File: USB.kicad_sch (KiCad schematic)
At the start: 8 parts, among them J7 USB-C, U8 USBLC6-2SC6

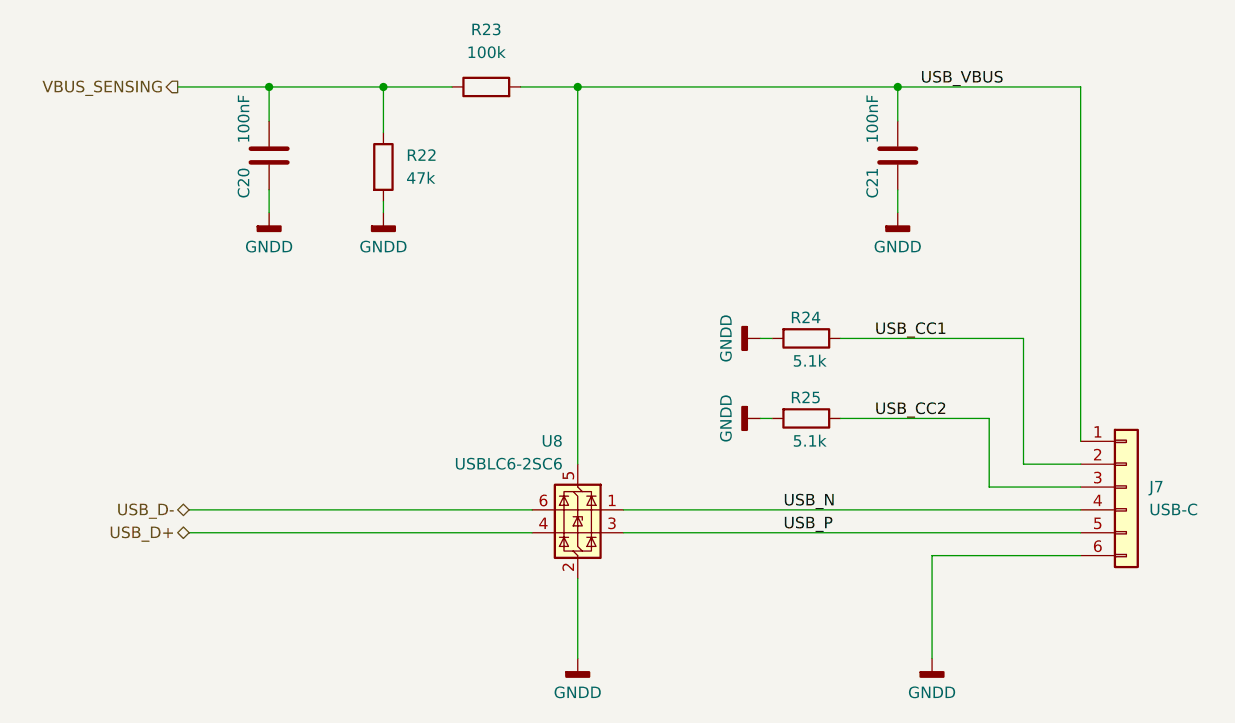
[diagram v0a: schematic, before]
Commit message: USB connector inversion fix
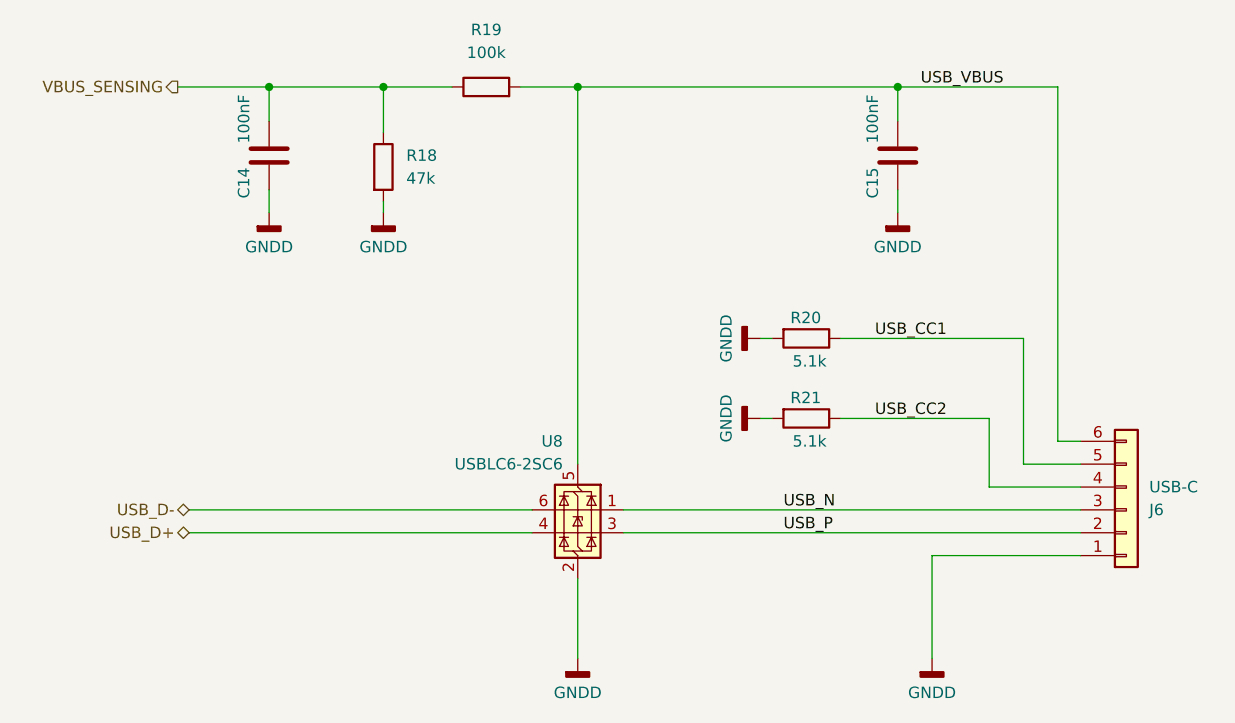
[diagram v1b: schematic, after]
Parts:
- renumbered C20 to C14, C21 to C15, J7 to J6, R22 to R18, R23 to R19, R24 to R20, R25 to R21
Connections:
- net GNDD: now also J6.1 (Pin_1); no longer J6.6 (Pin_6)
- net USB_CC1: now also J6.5 (Pin_5); no longer J6.2 (Pin_2)
- net USB_CC2: now also J6.4 (Pin_4); no longer J6.3 (Pin_3)
- net USB_N: now also J6.3 (Pin_3); no longer J6.4 (Pin_4)
- net USB_P: now also J6.2 (Pin_2); no longer J6.5 (Pin_5)
- net USB_VBUS: now also J6.6 (Pin_6); no longer J6.1 (Pin_1)
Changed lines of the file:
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@@
+	(wire
+		(pts
+			(xy 167.64 100.33) (xy 184.15 100.33)
+		)
+		(stroke
+			(width 0)
+			(type default)
+		)
+	)
+	(wire
+		(pts
+			(xy 83.82 48.26) (xy 106.68 48.26)
+		)
+		(stroke
+			(width 0)
+			(type default)
+		)
+	)
+	(wire
+		(pts
+			(xy 128.27 48.26) (xy 163.83 48.26)
+		)
+		(stroke
+			(width 0)
+			(type default)
+		)
+	)
+	(wire
+		(pts
+			(xy 128.27 102.87) (xy 128.27 111.76)
+		)
+		(stroke
+			(width 0)
+			(type default)
+		)
+	)
+	(wire
+		(pts
+			(xy 181.61 48.26) (xy 181.61 87.63)
+		)
+		(stroke
+			(width 0)
+			(type default)
+		)
+	)
+	(wire
+		(pts
+			(xy 157.48 85.09) (xy 173.99 85.09)
+		)
+		(stroke
+			(width 0)
+			(type default)
+		)
+	)
+	(wire
+		(pts
+			(xy 173.99 92.71) (xy 184.15 92.71)
+		)
+		(stroke
+			(width 0)
+			(type default)
+		)
+	)
+	(wire
+		(pts
+			(xy 121.92 48.26) (xy 128.27 48.26)
+		)
+		(stroke
+			(width 0)
+			(type default)
+		)
+	)
+	(wire
+		(pts
+			(xy 163.83 59.69) (xy 163.83 62.23)
+		)
+		(stroke
+			(width 0)
+			(type default)
+		)
+	)
 	(wire
 		(pts
@@
 	(wire
 		(pts
-			(xy 83.82 48.26) (xy 106.68 48.26)
-		)
-		(stroke
-			(width 0)
-			(type default)
-		)
-	)
-	(wire
-		(pts
-			(xy 128.27 48.26) (xy 163.83 48.26)
-		)
-		(stroke
-			(width 0)
-			(type default)
-		)
-	)
-	(wire
-		(pts
-			(xy 128.27 102.87) (xy 128.27 111.76)
-		)
-		(stroke
-			(width 0)
-			(type default)
-		)
-	)
-	(wire
-		(pts
-			(xy 184.15 48.26) (xy 184.15 87.63)
-		)
-		(stroke
-			(width 0)
-			(type default)
-		)
-	)
-	(wire
-		(pts
-			(xy 157.48 85.09) (xy 173.99 85.09)
-		)
-		(stroke
-			(width 0)
-			(type default)
-		)
-	)
-	(wire
-		(pts
-			(xy 121.92 48.26) (xy 128.27 48.26)
-		)
-		(stroke
-			(width 0)
-			(type default)
-		)
-	)
-	(wire
-		(pts
-			(xy 173.99 92.71) (xy 184.15 92.71)
-		)
-		(stroke
-			(width 0)
-			(type default)
-		)
-	)
-	(wire
-		(pts
-			(xy 163.83 59.69) (xy 163.83 62.23)
-		)
-		(stroke
-			(width 0)
-			(type default)
-		)
-	)
-	(wire
-		(pts
 			(xy 157.48 76.2) (xy 177.8 76.2)
 		)
@@
 	(wire
 		(pts
-			(xy 184.15 48.26) (xy 163.83 48.26)
+			(xy 181.61 48.26) (xy 163.83 48.26)
+		)
+		(stroke
+			(width 0)
+			(type default)
+		)
+	)
+	(wire
+		(pts
+			(xy 181.61 87.63) (xy 184.15 87.63)
 		)
 		(stroke
@@
 	(wire
 		(pts
+			(xy 133.35 97.79) (xy 184.15 97.79)
+		)
+		(stroke
+			(width 0)
+			(type default)
+		)
+	)
+	(wire
+		(pts
 			(xy 149.86 76.2) (xy 148.59 76.2)
 		)
@@
 	(wire
 		(pts
-			(xy 133.35 97.79) (xy 184.15 97.79)
-		)
-		(stroke
-			(width 0)
-			(type default)
-		)
-	)
-	(wire
-		(pts
 			(xy 114.3 48.26) (xy 106.68 48.26)
 		)
@@
 		(pts
 			(xy 93.98 48.26) (xy 93.98 52.07)
-		)
-		(stroke
-			(width 0)
-			(type default)
-		)
-	)
-	(wire
-		(pts
-			(xy 167.64 100.33) (xy 184.15 100.33)
 		)
 		(stroke
@@
 		(dnp no)
 		(fields_autoplaced yes)
-		(property "Reference" "#PWR036"
+		(property "Reference" "#PWR032"
 			(at 142.24 85.09 0)
 			(hide yes)
@@
 			(project "GSMreceiver"
 				(path "/bbc92722-7b85-49e8-a662-589426df605a/e36e7992-f69d-4591-9880-6ae3c36efe0e"
-					(reference "#PWR036")
+					(reference "#PWR032")
 					(unit 1)
 				)
@@
 		(dnp no)
 		(fields_autoplaced yes)
-		(property "Reference" "#PWR034"
+		(property "Reference" "#PWR030"
 			(at 128.27 118.11 0)
 			(hide yes)
@@
 			(project "GSMreceiver"
 				(path "/bbc92722-7b85-49e8-a662-589426df605a/e36e7992-f69d-4591-9880-6ae3c36efe0e"
-					(reference "#PWR034")
+					(reference "#PWR030")
 					(unit 1)
 				)
@@
 		(dnp no)
 		(fields_autoplaced yes)
-		(property "Reference" "#PWR032"
+		(property "Reference" "#PWR028"
 			(at 93.98 68.58 0)
 			(hide yes)
@@
 			(project "GSMreceiver"
 				(path "/bbc92722-7b85-49e8-a662-589426df605a/e36e7992-f69d-4591-9880-6ae3c36efe0e"
-					(reference "#PWR032")
+					(reference "#PWR028")
 					(unit 1)
 				)
@@
 		(dnp no)
 		(fields_autoplaced yes)
-		(property "Reference" "R23"
+		(property "Reference" "R19"
 			(at 118.11 41.91 90)
 			(show_name no)
@@
 			(project "GSMreceiver"
 				(path "/bbc92722-7b85-49e8-a662-589426df605a/e36e7992-f69d-4591-9880-6ae3c36efe0e"
-					(reference "R23")
+					(reference "R19")
 					(unit 1)
 				)
@@
 		(in_pos_files yes)
 		(dnp no)
-		(property "Reference" "C20"
+		(property "Reference" "C14"
 			(at 91.186 58.928 90)
 			(show_name no)
@@
 			(project "GSMreceiver"
 				(path "/bbc92722-7b85-49e8-a662-589426df605a/e36e7992-f69d-4591-9880-6ae3c36efe0e"
-					(reference "C20")
+					(reference "C14")
 					(unit 1)
 				)
@@
 		(dnp no)
 		(fields_autoplaced yes)
-		(property "Reference" "R22"
+		(property "Reference" "R18"
 			(at 109.22 55.8799 0)
 			(show_name no)
@@
 			(project "GSMreceiver"
 				(path "/bbc92722-7b85-49e8-a662-589426df605a/e36e7992-f69d-4591-9880-6ae3c36efe0e"
-					(reference "R22")
+					(reference "R18")
 					(unit 1)
 				)
@@
 		(dnp no)
 		(fields_autoplaced yes)
-		(property "Reference" "#PWR033"
+		(property "Reference" "#PWR029"
 			(at 106.68 68.58 0)
 			(hide yes)
@@
 			(project "GSMreceiver"
 				(path "/bbc92722-7b85-49e8-a662-589426df605a/e36e7992-f69d-4591-9880-6ae3c36efe0e"
-					(reference "#PWR033")
+					(reference "#PWR029")
 					(unit 1)
 				)
@@
 		(in_pos_files yes)
 		(dnp no)
-		(property "Reference" "C21"
+		(property "Reference" "C15"
 			(at 161.036 58.928 90)
 			(show_name no)
@@
 			(project "GSMreceiver"
 				(path "/bbc92722-7b85-49e8-a662-589426df605a/e36e7992-f69d-4591-9880-6ae3c36efe0e"
-					(reference "C21")
+					(reference "C15")
 					(unit 1)
 				)
@@
 		(dnp no)
 		(fields_autoplaced yes)
-		(property "Reference" "#PWR037"
+		(property "Reference" "#PWR033"
 			(at 163.83 68.58 0)
 			(hide yes)
@@
 			(project "GSMreceiver"
 				(path "/bbc92722-7b85-49e8-a662-589426df605a/e36e7992-f69d-4591-9880-6ae3c36efe0e"
-					(reference "#PWR037")
+					(reference "#PWR033")
 					(unit 1)
 				)
@@
 		(dnp no)
 		(fields_autoplaced yes)
-		(property "Reference" "#PWR038"
+		(property "Reference" "#PWR034"
 			(at 167.64 118.11 0)
 			(hide yes)
@@
 			(project "GSMreceiver"
 				(path "/bbc92722-7b85-49e8-a662-589426df605a/e36e7992-f69d-4591-9880-6ae3c36efe0e"
-					(reference "#PWR038")
+					(reference "#PWR034")
 					(unit 1)
 				)
@@
 		(in_pos_files yes)
 		(dnp no)
-		(property "Reference" "R25"
+		(property "Reference" "R21"
 			(at 151.892 82.804 90)
 			(show_name no)
@@
 			(project "GSMreceiver"
 				(path "/bbc92722-7b85-49e8-a662-589426df605a/e36e7992-f69d-4591-9880-6ae3c36efe0e"
-					(reference "R25")
+					(reference "R21")
 					(unit 1)
 				)
@@
 		(in_pos_files yes)
 		(dnp no)
-		(property "Reference" "R24"
+		(property "Reference" "R20"
 			(at 151.892 73.914 90)
 			(show_name no)
@@
 			(project "GSMreceiver"
 				(path "/bbc92722-7b85-49e8-a662-589426df605a/e36e7992-f69d-4591-9880-6ae3c36efe0e"
-					(reference "R24")
+					(reference "R20")
 					(unit 1)
 				)
@@
 	(symbol
 		(lib_id "Connector_Generic:Conn_01x06")
-		(at 189.23 92.71 0)
+		(at 189.23 95.25 0)
+		(mirror x)
 		(unit 1)
 		(body_style 1)
@@
 		(in_pos_files yes)
 		(dnp no)
-		(fields_autoplaced yes)
-		(property "Reference" "J7"
-			(at 191.77 92.7099 0)
+		(property "Reference" "J6"
+			(at 191.77 95.2501 0)
 			(show_name no)
 			(do_not_autoplace no)
@@
 		)
 		(property "Value" "USB-C"
-			(at 191.77 95.2499 0)
+			(at 191.77 92.7101 0)
 			(show_name no)
 			(do_not_autoplace no)
@@
 		)
 		(property "Footprint" "Connector_JST:JST_PH_B6B-PH-K_1x06_P2.00mm_Vertical"
-			(at 189.23 92.71 0)
+			(at 189.23 95.25 0)
 			(hide yes)
 			(show_name no)
@@
 		)
 		(property "Datasheet" ""
-			(at 189.23 92.71 0)
+			(at 189.23 95.25 0)
 			(hide yes)
 			(show_name no)
@@
 		)
 		(property "Description" "Generic connector, single row, 01x06, script generated (kicad-library-utils/schlib/autogen/connector/)"
-			(at 189.23 92.71 0)
+			(at 189.23 95.25 0)
 			(hide yes)
 			(show_name no)
@@
 		)
 		(property "Manufacturer" "JST"
-			(at 189.23 92.71 0)
+			(at 189.23 95.25 0)
 			(hide yes)
 			(show_name no)
@@
 		)
 		(property "MPN" "B6B-PH-K"
-			(at 189.23 92.71 0)
+			(at 189.23 95.25 0)
 			(hide yes)
 			(show_name no)
@@
 			(project "GSMreceiver"
 				(path "/bbc92722-7b85-49e8-a662-589426df605a/e36e7992-f69d-4591-9880-6ae3c36efe0e"
-					(reference "J7")
+					(reference "J6")
 					(unit 1)
 				)
@@
 		(dnp no)
 		(fields_autoplaced yes)
-		(property "Reference" "#PWR035"
+		(property "Reference" "#PWR031"
 			(at 142.24 76.2 0)
 			(hide yes)
@@
 			(project "GSMreceiver"
 				(path "/bbc92722-7b85-49e8-a662-589426df605a/e36e7992-f69d-4591-9880-6ae3c36efe0e"
-					(reference "#PWR035")
+					(reference "#PWR031")
 					(unit 1)
 				)
